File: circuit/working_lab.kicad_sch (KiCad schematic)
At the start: 12 parts, among them J1 Screw_Terminal_01x02, J2 Conn_01x05, J3 Conn_01x03, J4 Conn_01x03, U1 PIC16F886-IP, U2 L7805, Y1 Crystal

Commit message: circuit in progress
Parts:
- removed C3: 0.1uF, Capacitor_THT:C_Disc_D3.8mm_W2.6mm_P2.50mm, symbol Device:C
- removed C4: 0.33uF, Capacitor_THT:C_Disc_D3.8mm_W2.6mm_P2.50mm, symbol Device:C
- removed R1: 5k, Resistor_THT:R_Axial_DIN0204_L3.6mm_D1.6mm_P5.08mm_Horizontal, symbol Device:R
- added C1: 0.33uF, Capacitor_THT:CP_Radial_D5.0mm_P2.50mm, symbol Device:C_Polarized_US
- added C2: 0.1uF, Capacitor_THT:CP_Radial_D5.0mm_P2.50mm, symbol Device:C_Polarized_US
- added R1: 5k, Resistor_THT:R_Axial_DIN0204_L3.6mm_D1.6mm_P7.62mm_Horizontal, symbol Device:R_US
- J3: value Conn_01x03 -> USART
- U2: footprint (none) -> Package_TO_SOT_THT:TO-220-3_Vertical
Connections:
- net +12V: now also C1.1
- net +5V: now also C2.1, R1.2
- net GND: now also C1.2, C2.2
- net mclr: now also R1.1
- net icsp_dat: now reaches J2.4 (Pin_4), U1.28 (ICSPDAT/RB7)
- net icsp_clk: now reaches J2.5 (Pin_5), U1.27 (ICSPCLK/RB6)

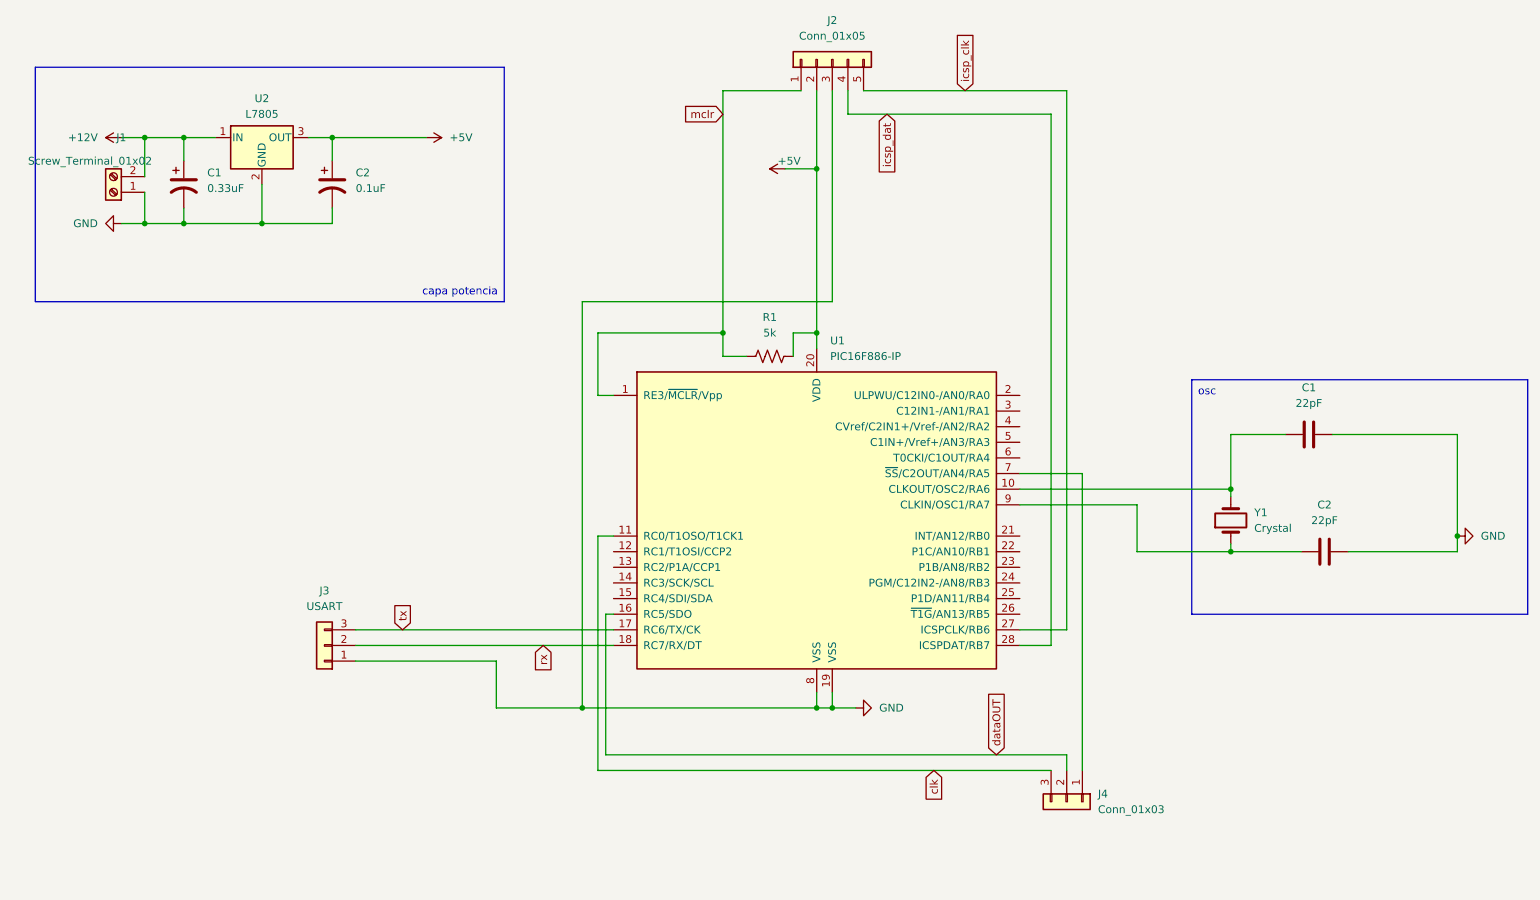
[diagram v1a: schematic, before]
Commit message: I2C connection in circuit created
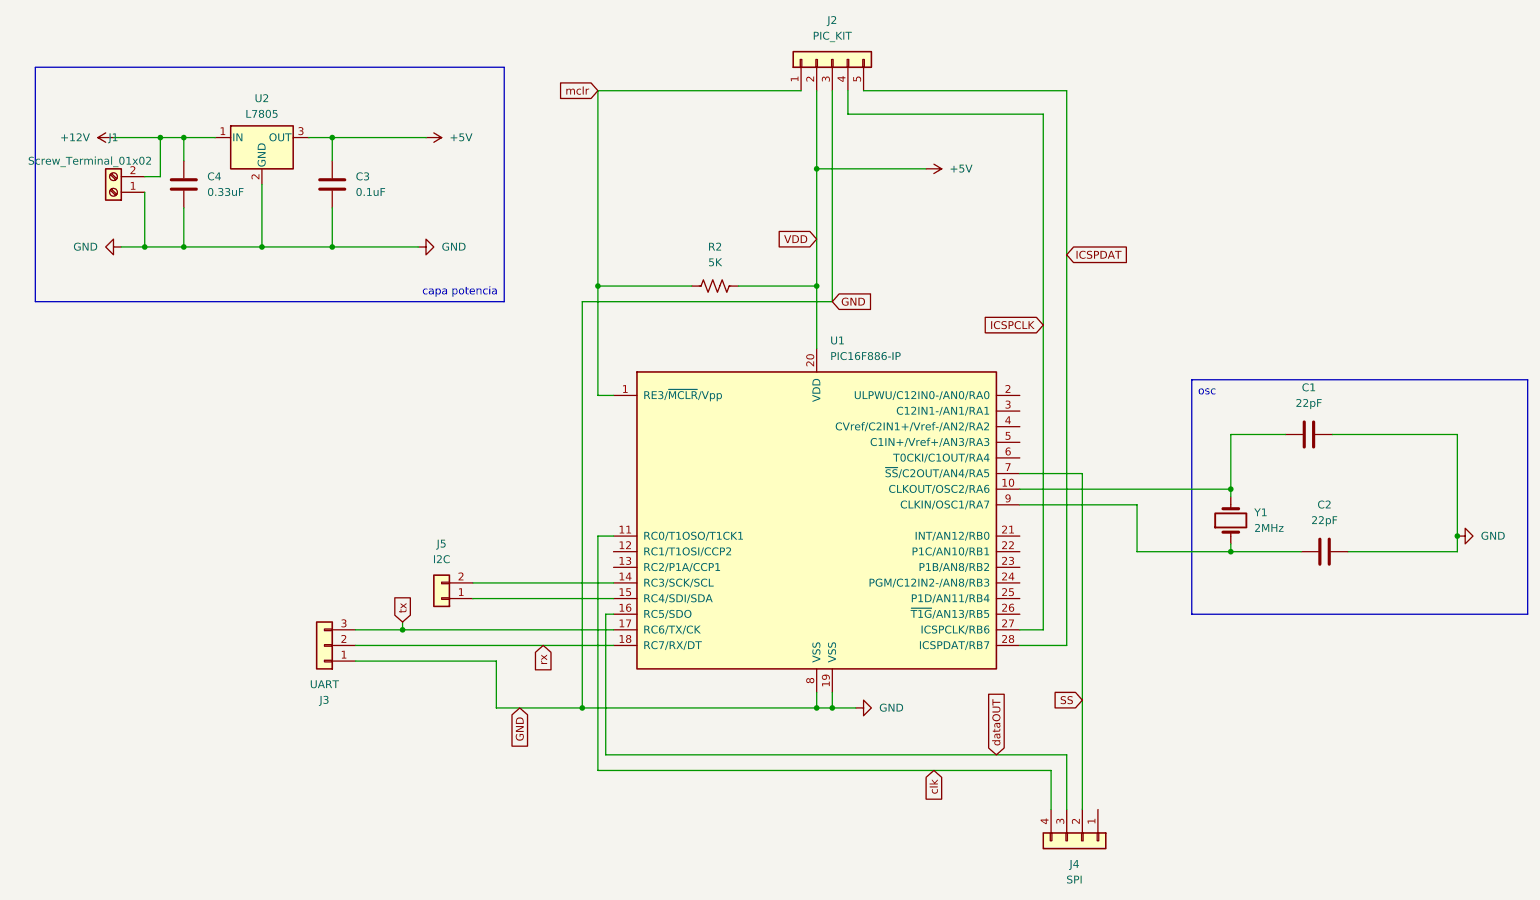
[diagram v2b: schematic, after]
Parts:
- removed C1: 0.33uF, Capacitor_THT:CP_Radial_D5.0mm_P2.50mm, symbol Device:C_Polarized_US
- removed C2: 0.1uF, Capacitor_THT:CP_Radial_D5.0mm_P2.50mm, symbol Device:C_Polarized_US
- removed J4: Conn_01x03, Connector_PinSocket_2.54mm:PinSocket_1x03_P2.54mm_Vertical, symbol Connector_Generic:Conn_01x03
- removed R1: 5k, Resistor_THT:R_Axial_DIN0204_L3.6mm_D1.6mm_P7.62mm_Horizontal, symbol Device:R_US
- added C3: 0.1uF, Capacitor_THT:C_Disc_D3.8mm_W2.6mm_P2.50mm, symbol Device:C
- added C4: 0.33uF, Capacitor_THT:CP_Radial_D5.0mm_P2.50mm, symbol Device:C
- added J4: SPI, Connector_PinSocket_1.00mm:PinSocket_1x04_P1.00mm_Vertical, symbol Connector_Generic:Conn_01x04
- added J5: I2C, Connector_PinSocket_2.54mm:PinSocket_1x02_P2.54mm_Vertical, symbol Connector_Generic:Conn_01x02
- added R2: 5K, Resistor_THT:R_Axial_DIN0204_L3.6mm_D1.6mm_P7.62mm_Horizontal, symbol Device:R_US
- J2: value Conn_01x05 -> PIC_KIT
- J3: value USART -> UART
- Y1: value Crystal -> 2MHz
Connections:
- net +12V: now also C4.2
- net +5V: now also C3.2, R2.2
- net GND: now also C3.1, C4.1
- net clk: now also J4.4 (Pin_4)
- net dataOUT: now also J4.3 (Pin_3)
- net mclr: now also R2.1
- net at U1.14 (RC3/SCK/SCL): now also J5.2 (Pin_2)
- net at U1.15 (RC4/SDI/SDA): now also J5.1 (Pin_1)
- net SS: now reaches U1.7 (~{SS}/C2OUT/AN4/RA5)
- net SS: now also J4.2 (Pin_2)
- net icsp_clk renamed ICSPCLK
- net ICSPCLK: now also J2.4 (Pin_4); no longer J2.5 (Pin_5)
- net icsp_dat renamed ICSPDAT
- net ICSPDAT: now also J2.5 (Pin_5); no longer J2.4 (Pin_4)

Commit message: circuit update
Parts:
- removed J4: SPI, Connector_PinSocket_1.00mm:PinSocket_1x04_P1.00mm_Vertical, symbol Connector_Generic:Conn_01x04
- added J4: SPI, Connector_PinSocket_2.54mm:PinSocket_1x02_P2.54mm_Vertical, symbol Connector_Generic:Conn_01x02
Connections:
- net clk: now also J4.2 (Pin_2)
- net dataOUT: now also J4.1 (Pin_1)
- net SS: no longer names the net of U1.7 (~{SS}/C2OUT/AN4/RA5)
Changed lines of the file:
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@@
-    (stroke (width 0) (type default))
-  )
-  (wire (pts (xy 180.34 88.9) (xy 190.5 88.9))
     (stroke (width 0) (type default))
   )
@@
   )
   (wire (pts (xy 95.25 127) (xy 109.22 127))
-    (stroke (width 0) (type default))
-  )
-  (wire (pts (xy 190.5 88.9) (xy 190.5 143.51))
     (stroke (width 0) (type default))
   )
@@
     (effects (font (size 1.27 1.27)) (justify right))
     (property "Intersheetrefs" "${INTERSHEET_REFS}" (at 173.2424 64.77 0)
-      (effects (font (size 1.27 1.27)) (justify right) hide)
-    )
-  )
-  (global_label "SS" (shape input) (at 190.5 125.73 180) (fields_autoplaced)
-    (effects (font (size 1.27 1.27)) (justify right))
-    (property "Intersheetrefs" "${INTERSHEET_REFS}" (at 185.0958 125.73 0)
       (effects (font (size 1.27 1.27)) (justify right) hide)
     )
@@
     )
   )
-  (symbol (lib_id "Connector_Generic:Conn_01x04") (at 190.5 148.59 270) (unit 1)
-    (in_bom yes) (on_board yes) (dnp no) (fields_autoplaced)
-    (property "Reference" "J4" (at 189.23 152.4 90)
-      (effects (font (size 1.27 1.27)))
-    )
-    (property "Value" "SPI" (at 189.23 154.94 90)
-      (effects (font (size 1.27 1.27)))
-    )
-    (property "Footprint" "Connector_PinSocket_1.00mm:PinSocket_1x04_P1.00mm_Vertical" (at 190.5 148.59 0)
-      (effects (font (size 1.27 1.27)) hide)
-    )
-    (property "Datasheet" "~" (at 190.5 148.59 0)
-      (effects (font (size 1.27 1.27)) hide)
-    )
-    (pin "1")
-    (pin "2")
-    (pin "3")
-    (pin "4")
-    (instances
-      (project "working_lab"
+  (symbol (lib_id "Connector_Generic:Conn_01x02") (at 187.96 148.59 270) (unit 1)
+    (in_bom yes) (on_board yes) (dnp no) (fields_autoplaced)
+    (property "Reference" "J4" (at 190.5 147.32 90)
+      (effects (font (size 1.27 1.27)) (justify left))
+    )
+    (property "Value" "SPI" (at 190.5 149.86 90)
+      (effects (font (size 1.27 1.27)) (justify left))
+    )
+    (property "Footprint" "Connector_PinSocket_2.54mm:PinSocket_1x02_P2.54mm_Vertical" (at 187.96 148.59 0)
+      (effects (font (size 1.27 1.27)) hide)
+    )
+    (property "Datasheet" "~" (at 187.96 148.59 0)
+      (effects (font (size 1.27 1.27)) hide)
+    )
+    (pin "1")
+    (pin "2")
+    (instances
+      (project "working_lab"

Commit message: circuit completed
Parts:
- added J6: PWM, Connector_PinSocket_2.54mm:PinSocket_1x01_P2.54mm_Vertical, symbol Connector_Generic:Conn_01x01
- added J7: Analogic, Connector_PinSocket_2.54mm:PinSocket_1x03_P2.54mm_Vertical, symbol Connector_Generic:Conn_01x03
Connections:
- net at U1.13 (RC2/P1A/CCP1): now also J6.1 (Pin_1)
- net at U1.21 (INT/AN12/RB0): now also J7.1 (Pin_1)
- net at U1.22 (P1C/AN10/RB1): now also J7.2 (Pin_2)
- net at U1.23 (P1B/AN8/RB2): now also J7.3 (Pin_3)
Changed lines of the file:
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@@
+    (stroke (width 0) (type default))
+  )
+  (wire (pts (xy 180.34 99.06) (xy 189.23 99.06))
     (stroke (width 0) (type default))
   )
@@
     (stroke (width 0) (type default))
   )
+  (wire (pts (xy 180.34 101.6) (xy 189.23 101.6))
+    (stroke (width 0) (type default))
+  )
+  (wire (pts (xy 180.34 104.14) (xy 189.23 104.14))
+    (stroke (width 0) (type default))
+  )
   (wire (pts (xy 113.03 134.62) (xy 113.03 111.76))
     (stroke (width 0) (type default))
@@
   )
   (wire (pts (xy 153.67 127) (xy 149.86 127))
+    (stroke (width 0) (type default))
+  )
+  (wire (pts (xy 114.3 104.14) (xy 100.33 104.14))
     (stroke (width 0) (type default))
   )
@@
         (path "/dfeec936-19a0-43aa-aa56-37214232a158"
           (reference "C4") (unit 1)
+        )
+      )
+    )
+  )
+  (symbol (lib_id "Connector_Generic:Conn_01x03") (at 194.31 101.6 0) (unit 1)
+    (in_bom yes) (on_board yes) (dnp no)
+    (property "Reference" "J7" (at 196.85 100.33 0)
+      (effects (font (size 1.27 1.27)) (justify left))
+    )
+    (property "Value" "Analogic" (at 190.5 106.68 0)
+      (effects (font (size 1.27 1.27)) (justify left))
+    )
+    (property "Footprint" "Connector_PinSocket_2.54mm:PinSocket_1x03_P2.54mm_Vertical" (at 194.31 101.6 0)
+      (effects (font (size 1.27 1.27)) hide)
+    )
+    (property "Datasheet" "~" (at 194.31 101.6 0)
+      (effects (font (size 1.27 1.27)) hide)
+    )
+    (pin "1")
+    (pin "2")
+    (pin "3")
+    (instances
+      (project "working_lab"
+        (path "/dfeec936-19a0-43aa-aa56-37214232a158"
+          (reference "J7") (unit 1)
         )
       )
@@
         )
       )
+    )
+  )
+  (symbol (lib_id "Connector_Generic:Conn_01x01") (at 95.25 104.14 180) (unit 1)
+    (in_bom yes) (on_board yes) (dnp no) (fields_autoplaced)
+    (property "Reference" "J6" (at 95.25 97.79 0)
+      (effects (font (size 1.27 1.27)))
+    )
+    (property "Value" "PWM" (at 95.25 100.33 0)
+      (effects (font (size 1.27 1.27)))
+    )
+    (property "Footprint" "Connector_PinSocket_2.54mm:PinSocket_1x01_P2.54mm_Vertical" (at 95.25 104.14 0)
+      (effects (font (size 1.27 1.27)) hide)
+    )
+    (property "Datasheet" "~" (at 95.25 104.14 0)
+      (effects (font (size 1.27 1.27)) hide)
+    )
+    (pin "1")
+    (instances
+      (project "working_lab"
+        (path "/dfeec936-19a0-43aa-aa56-37214232a158"
+          (reference "J6") (unit 1)
+        )
+      )
